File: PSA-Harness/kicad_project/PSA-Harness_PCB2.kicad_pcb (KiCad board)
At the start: 4 copper layers, 27.4 x 53.6 mm, 10 parts, among them J1 to_EPS_1, J2 to_EPS_2, J3 to_ESP_3, J7 USB_C_Receptacle, J8 B2B_1, J9 B2B_2, K1 G6K-2G-Y DC5

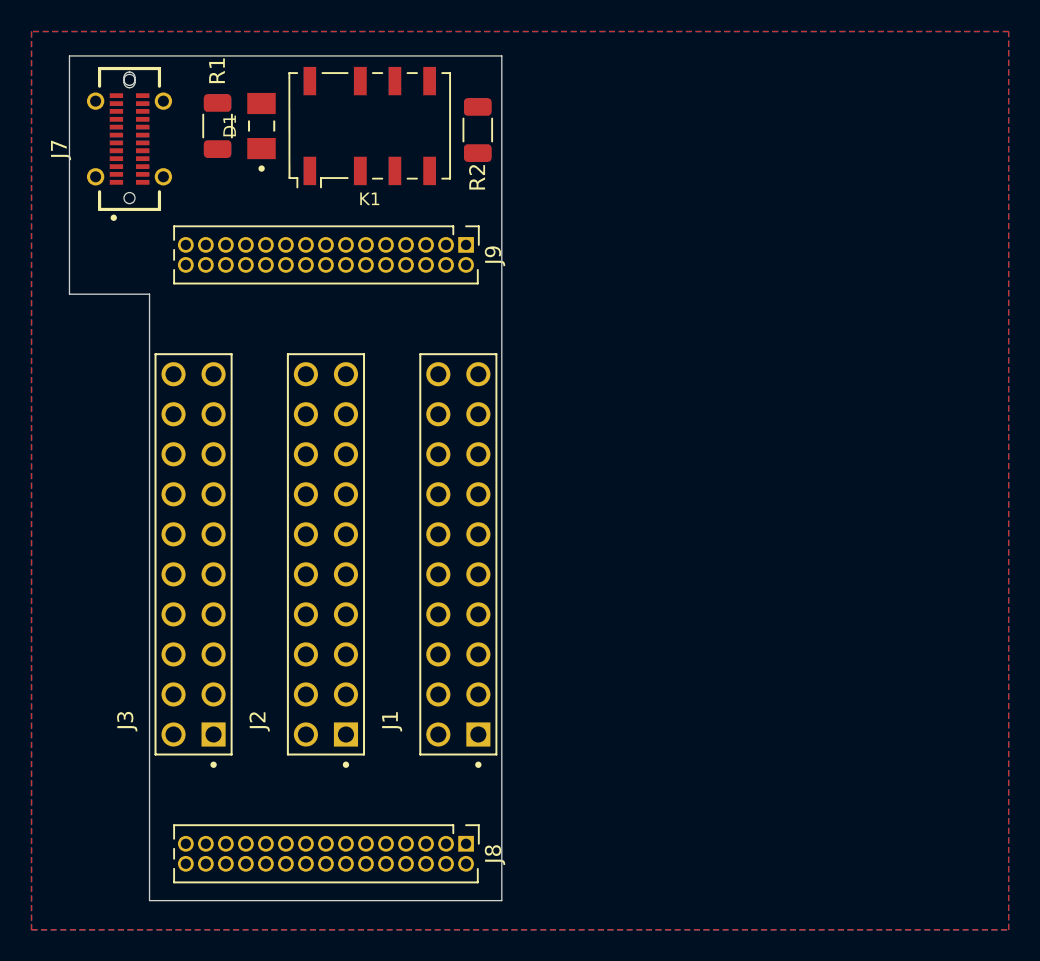
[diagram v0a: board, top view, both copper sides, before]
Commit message: PCB1 routed, PCB2 partly routed
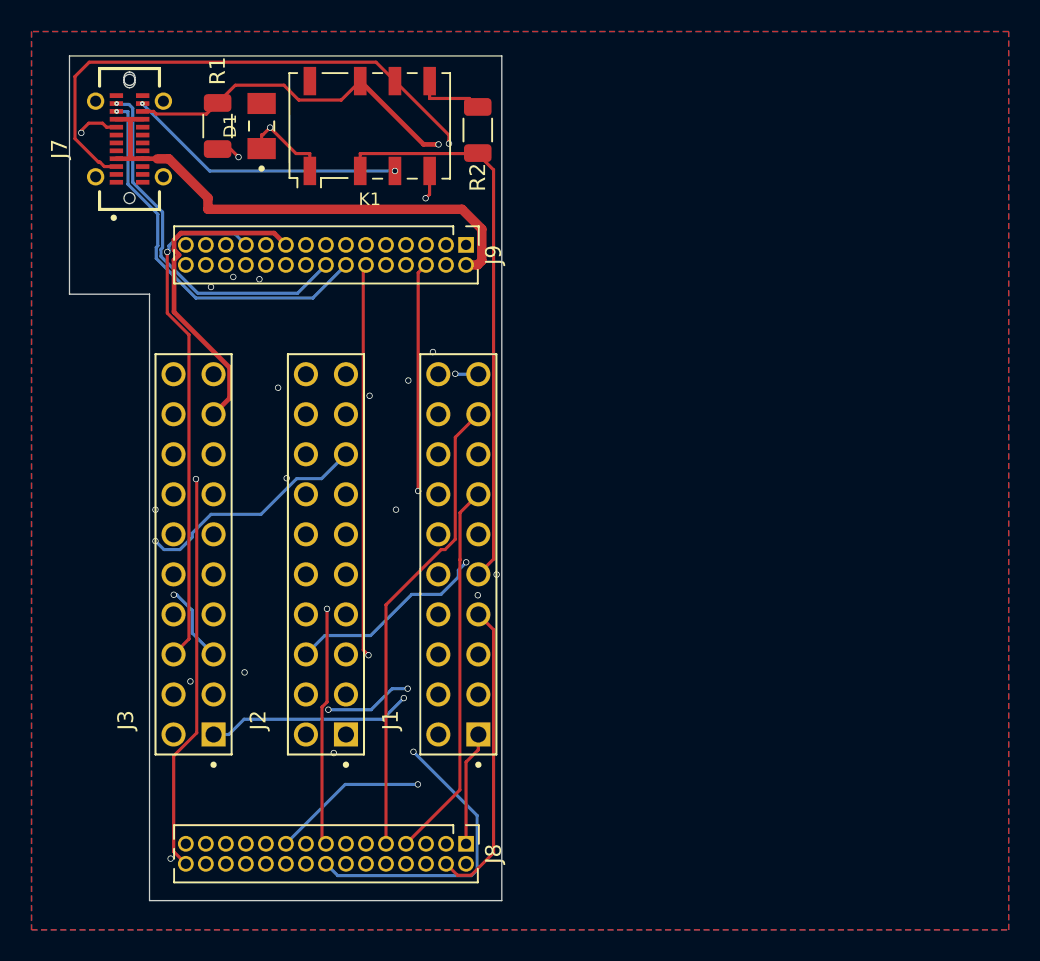
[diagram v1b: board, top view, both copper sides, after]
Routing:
- net CAN2_L: track 0.00 -> 73.9 mm, vias 0 -> 1
- net CAN0_L: track 0.00 -> 69.5 mm, vias 0 -> 1
- net +12V: track 0.00 -> 64.9 mm
- net 41: track 0.00 -> 53.0 mm, vias 0 -> 2
- net 20: track 0.00 -> 52.1 mm, vias 0 -> 3
- net CAN1_L: track 0.00 -> 50.5 mm, vias 0 -> 1
- net 43: track 0.00 -> 44.4 mm, vias 0 -> 2
- net 10: track 0.00 -> 43.5 mm, vias 0 -> 3
- net 51: track 0.00 -> 41.4 mm, vias 0 -> 1
- net 45: track 0.00 -> 39.4 mm, vias 0 -> 1
- net 28: track 0.00 -> 38.8 mm, vias 0 -> 1
- net 30: track 0.00 -> 37.6 mm, vias 0 -> 1
- net 33: track 0.00 -> 37.5 mm, vias 0 -> 1
- net CAN0_H: track 0.00 -> 36.1 mm
- net 42: track 0.00 -> 35.8 mm, vias 0 -> 1
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
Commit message: chg: rearrange pcb interconnect pins
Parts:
- moved J8 38.0 mm to (114.6, 102.5)
- moved J9 38.0 mm to (114.6, 140.5)
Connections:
- J8 pad 1: 1 -> 11
- J8 pad 10: 10 -> 16
- J8 pad 11: 11 -> 6
- J8 pad 12: 12 -> 17
- J8 pad 13: 13 -> 4
- J8 pad 14: 14 -> 18
- J8 pad 15: 15 -> 2
- J8 pad 16: 16 -> 19
- J8 pad 17: 17 -> 1
- J8 pad 18: 18 -> 20
- J8 pad 19: 19 -> CAN2_H
- J8 pad 2: 2 -> 12
- J8 pad 20: 20 -> 21
- J8 pad 21: 21 -> CAN2_L
- J8 pad 23: 23 -> CAN1_H
- J8 pad 24: GND -> 23
- J8 pad 25: 25 -> CAN1_L
- J8 pad 26: 26 -> 25
- J8 pad 27: 27 -> GND
- J8 pad 28: 28 -> 26
- J8 pad 29: 29 -> +12V
- J8 pad 3: CAN2_L -> 10
- J8 pad 30: 30 -> 27
- J8 pad 4: 4 -> 13
- J8 pad 5: CAN2_H -> 9
- J8 pad 6: 6 -> 14
- J8 pad 7: 7 -> 8
- J8 pad 8: 8 -> 15
- J8 pad 9: 9 -> 7
- J9 pad 1: 31 -> 43
- J9 pad 10: 40 -> 50
- J9 pad 11: 41 -> 38
- J9 pad 12: 42 -> 51
- J9 pad 13: 43 -> 37
- J9 pad 14: CAN1_L -> 52
- J9 pad 15: 45 -> 36
- J9 pad 16: CAN1_H -> 53
- J9 pad 17: 47 -> 35
- J9 pad 18: 48 -> 54
- J9 pad 19: 49 -> 34
- J9 pad 2: +12V -> 45
- J9 pad 20: 50 -> 55
- J9 pad 21: 51 -> 33
- J9 pad 22: 52 -> 56
- J9 pad 23: 53 -> 31
- J9 pad 24: 54 -> 57
- J9 pad 25: 55 -> 30
- J9 pad 26: 56 -> 58
- J9 pad 27: 57 -> 29
- J9 pad 28: 58 -> 59
- J9 pad 29: 59 -> 28
- J9 pad 3: 33 -> 42
- J9 pad 4: 34 -> 47
- J9 pad 5: 35 -> 41
- J9 pad 6: 36 -> 48
- J9 pad 7: 37 -> 40
- J9 pad 8: 38 -> 49
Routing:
- net CAN2_L: track 73.9 -> 0.00 mm, vias 1 -> 0
- net CAN0_L: track 69.5 -> 0.00 mm, vias 1 -> 0
- net +12V: track 64.9 -> 0.00 mm
- net 41: track 53.0 -> 0.00 mm, vias 2 -> 0
- net 20: track 52.1 -> 0.00 mm, vias 3 -> 0
- net CAN1_L: track 50.5 -> 0.00 mm, vias 1 -> 0
- net 43: track 44.4 -> 0.00 mm, vias 2 -> 0
- net 10: track 43.5 -> 0.00 mm, vias 3 -> 0
- net 51: track 41.4 -> 0.00 mm, vias 1 -> 0
- net 45: track 39.4 -> 0.00 mm, vias 1 -> 0
- net 28: track 38.8 -> 0.00 mm, vias 1 -> 0
- net 30: track 37.6 -> 0.00 mm, vias 1 -> 0
- net 33: track 37.5 -> 0.00 mm, vias 1 -> 0
- net CAN0_H: track 36.1 -> 0.00 mm
- net 42: track 35.8 -> 0.00 mm, vias 1 -> 0
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
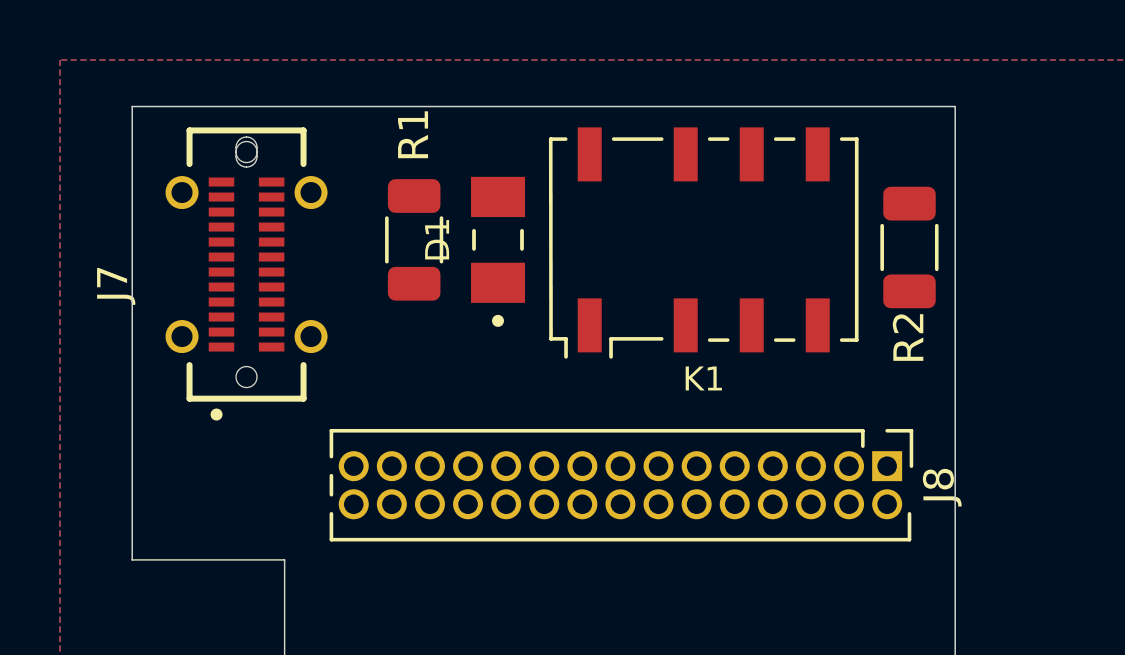
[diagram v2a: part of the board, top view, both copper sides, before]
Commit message: PCB1 routed, PCB2 partly
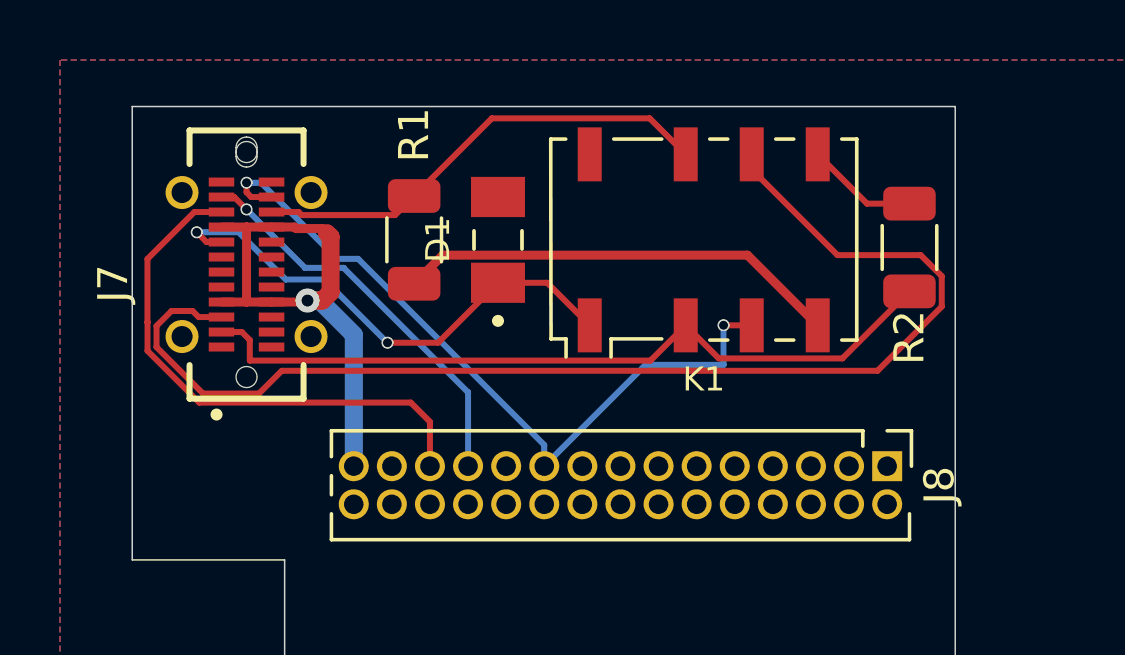
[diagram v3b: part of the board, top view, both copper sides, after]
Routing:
- net CAN0_L: track 0.00 -> 40.5 mm
- net CAN0_H: track 0.00 -> 25.6 mm
- net CAN2_H: track 0.00 -> 25.1 mm, vias 0 -> 2
- net +12V: track 0.00 -> 18.3 mm, vias 0 -> 1
- net CAN1_L: track 0.00 -> 18.1 mm
- net SBU1: track 0.00 -> 17.0 mm, vias 0 -> 2
- net CAN2_L: track 0.00 -> 15.7 mm
- net Net-(K1-Pad4): track 0.00 -> 14.8 mm
- net CAN1_H: track 0.00 -> 13.4 mm, vias 0 -> 1
- net Net-(K1-Pad5): track 0.00 -> 3.74 mm

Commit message: PCB1+2 routed
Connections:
- J7 pad S2: (no net) -> GND
- J7 pad S3: (no net) -> GND
- J7 pad S4: (no net) -> GND
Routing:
- net 50: track 0.00 -> 52.7 mm, vias 0 -> 4
- net 4: track 0.00 -> 49.6 mm, vias 0 -> 3
- net 1: track 0.00 -> 46.8 mm, vias 0 -> 1
- net 48: track 0.00 -> 45.0 mm, vias 0 -> 1
- net 29: track 0.00 -> 44.3 mm, vias 0 -> 1
- net 49: track 0.00 -> 41.6 mm
- net 2: track 0.00 -> 41.6 mm, vias 0 -> 1
- net 58: track 0.00 -> 36.8 mm, vias 0 -> 1
- net CAN0_L: track 40.5 -> 77.2 mm, vias 0 -> 4
- net 47: track 0.00 -> 36.6 mm
- net 28: track 0.00 -> 36.4 mm, vias 0 -> 1
- net 30: track 0.00 -> 35.9 mm, vias 0 -> 1
- net 40: track 0.00 -> 33.2 mm
- net +12V: track 18.3 -> 51.1 mm
- net 11: track 0.00 -> 32.4 mm, vias 0 -> 1
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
